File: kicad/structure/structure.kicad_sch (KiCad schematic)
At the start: 12 parts, among them J10 Conn_01x04_Socket, J11 Conn_01x04_Socket, J12 Conn_01x03_Socket, J13 Conn_01x06_Socket, J14 Conn_01x06_Socket, J3 Conn_01x08_Socket, J4 Conn_01x05_Socket, J5 Conn_01x03_Socket, J6 Conn_01x06_Socket, J7 Conn_01x04_Socket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

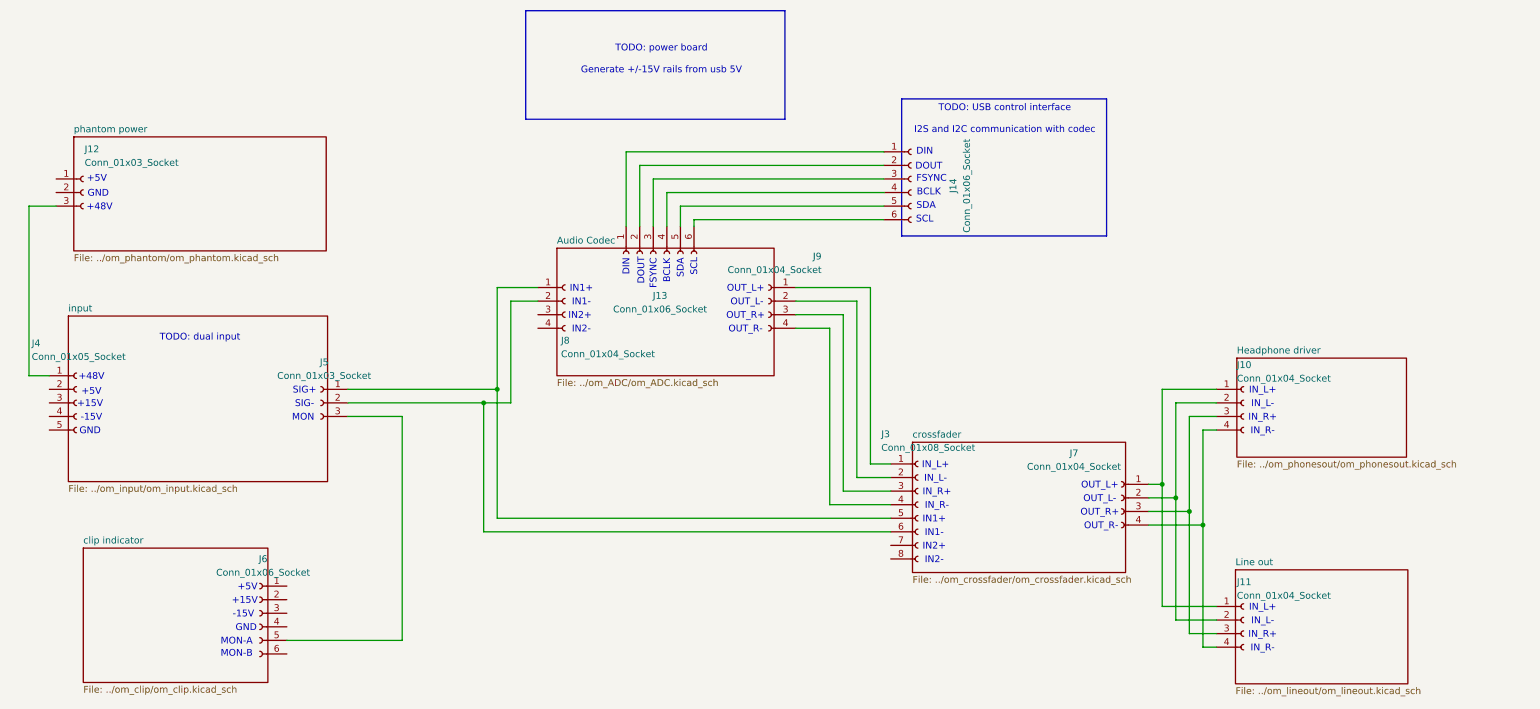
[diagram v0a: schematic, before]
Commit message: added structure and dual input
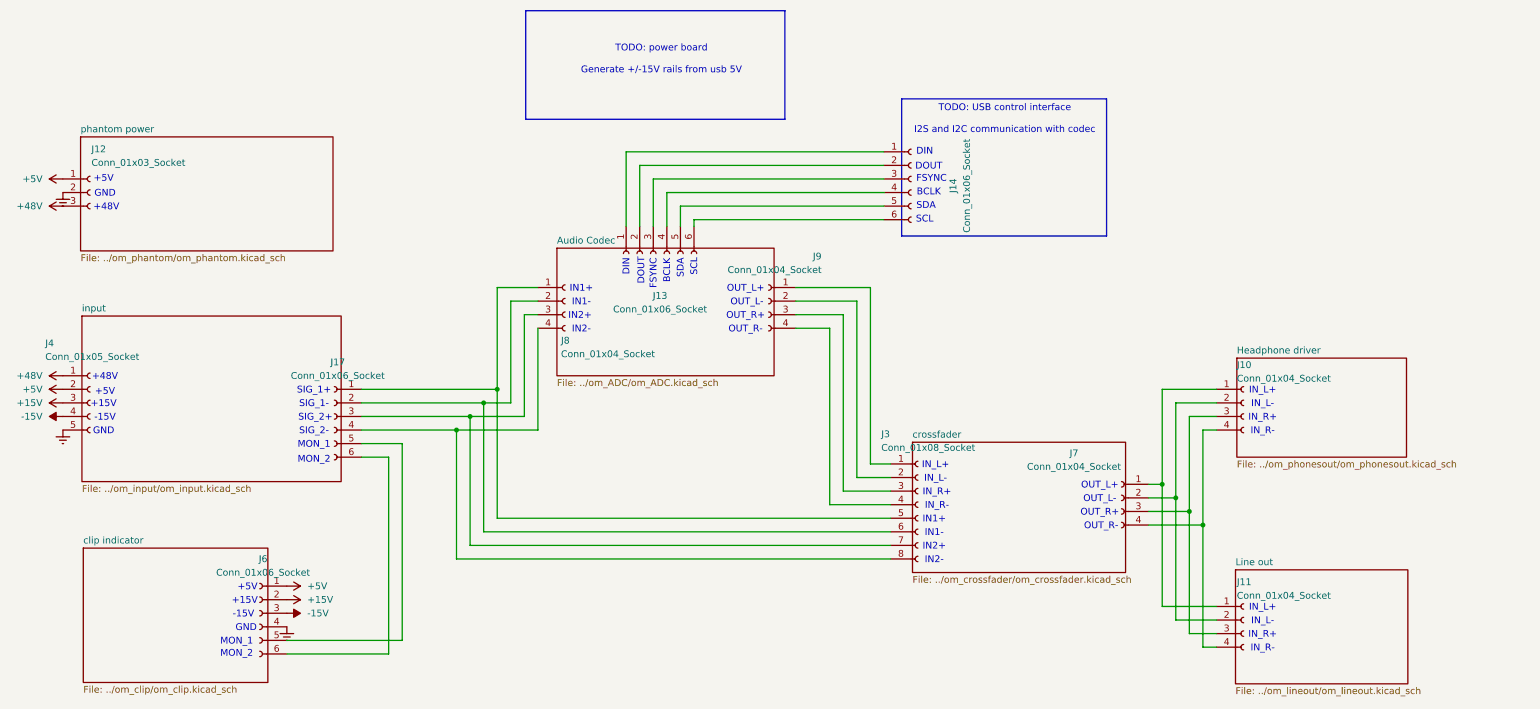
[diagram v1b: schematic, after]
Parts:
- removed J5: Conn_01x03_Socket, symbol Connector:Conn_01x03_Socket
- added J17: Conn_01x06_Socket, symbol Connector:Conn_01x06_Socket
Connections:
- net +48V: now reaches J12.3 (Pin_3), J4.1 (Pin_1)
- net +5V: now reaches J4.2 (Pin_2)
- net +5V: now also J12.1 (Pin_1), J6.1 (Pin_1)
- net +15V: now reaches J4.3 (Pin_3)
- net +15V: now also J6.2 (Pin_2)
- net -15V: now reaches J4.4 (Pin_4)
- net -15V: now also J6.3 (Pin_3)
- net Earth: now reaches J4.5 (Pin_5)
- net Earth: now also J12.2 (Pin_2), J6.4 (Pin_4)
- net at J3.5 (Pin_5), J8.1 (Pin_1): now also J17.1 (Pin_1)
- net at J3.6 (Pin_6), J8.2 (Pin_2): now also J17.2 (Pin_2)
- net at J8.3 (Pin_3): now also J3.7 (Pin_7), J17.3 (Pin_3)
- net at J8.4 (Pin_4): now also J3.8 (Pin_8), J17.4 (Pin_4)
- net at J6.5 (Pin_5): now also J17.5 (Pin_5)
- net at J6.6 (Pin_6): now also J17.6 (Pin_6)
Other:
- note added: "MON_1"
- note added: "MON_2"
- note added: "SIG_1+"
- note added: "SIG_1-"
- note added: "SIG_2+"
- note added: "SIG_2-"
- note removed: "MON"
- note removed: "MON-A"
- note removed: "MON-B"
- note removed: "SIG+"
- note removed: "SIG-"
- note removed: "TODO: dual input"
- moved on the sheet: J12, J4

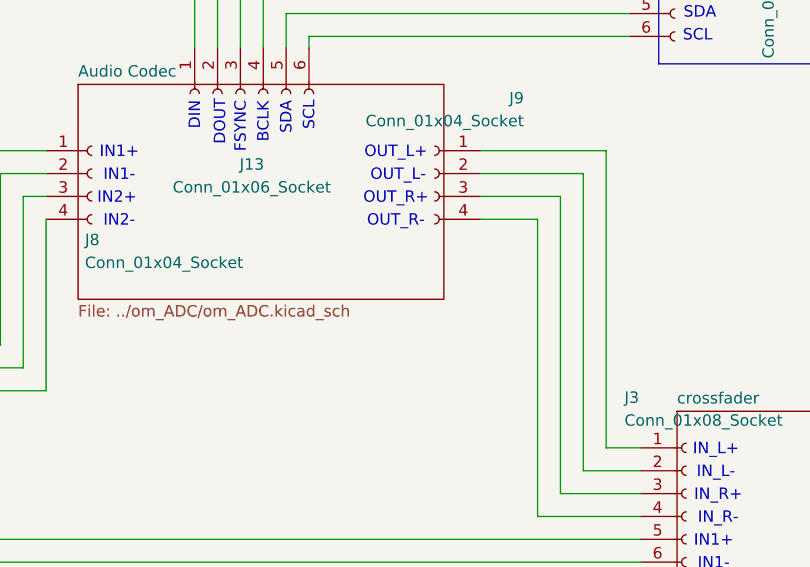
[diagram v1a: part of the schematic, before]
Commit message: direct monitor switch (#5)
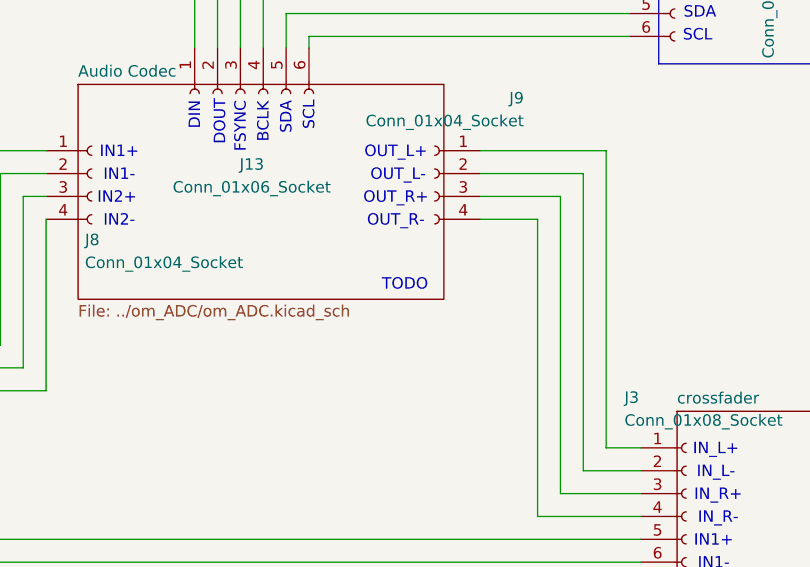
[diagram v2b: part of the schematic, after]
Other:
- note added: "TODO"
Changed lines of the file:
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@@
+		)
+	)
+	(text "TODO"
+		(exclude_from_sim no)
+		(at 151.638 89.916 0)
+		(effects
+			(font
+				(size 1.27 1.27)
+			)
 		)
 	)

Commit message: net labels
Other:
- note added: "phantom"
- note removed: "+48V"
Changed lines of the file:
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@@
 		)
 	)
-	(text "+48V"
+	(text "phantom"
 		(exclude_from_sim no)
-		(at 30.734 91.694 0)
+		(at 33.02 91.694 0)
 		(effects
 			(font
@@
 		)
 	)
-	(text "+48V"
+	(text "phantom"
 		(exclude_from_sim no)
-		(at 30.988 59.944 0)
+		(at 33.02 59.944 0)
 		(effects
 			(font

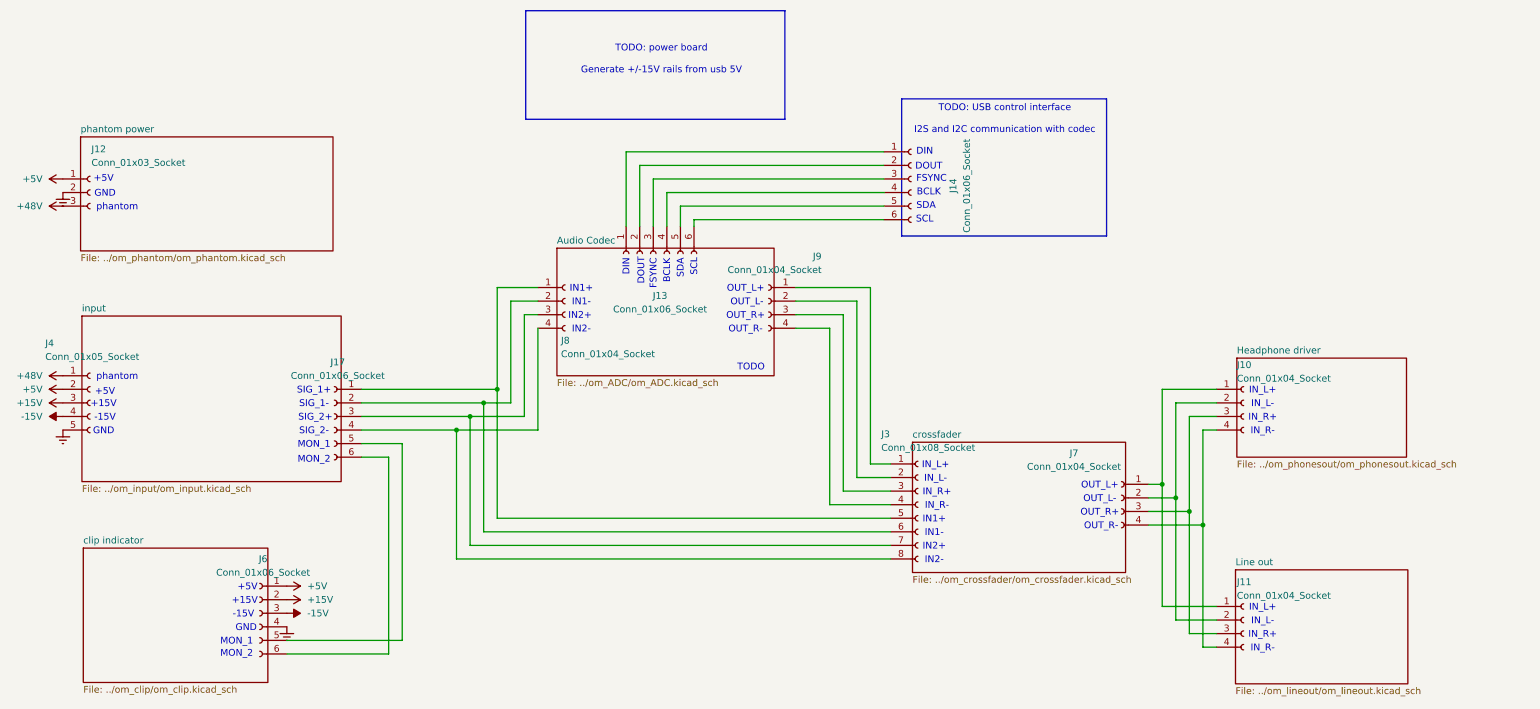
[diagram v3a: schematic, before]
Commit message: line output gain staging
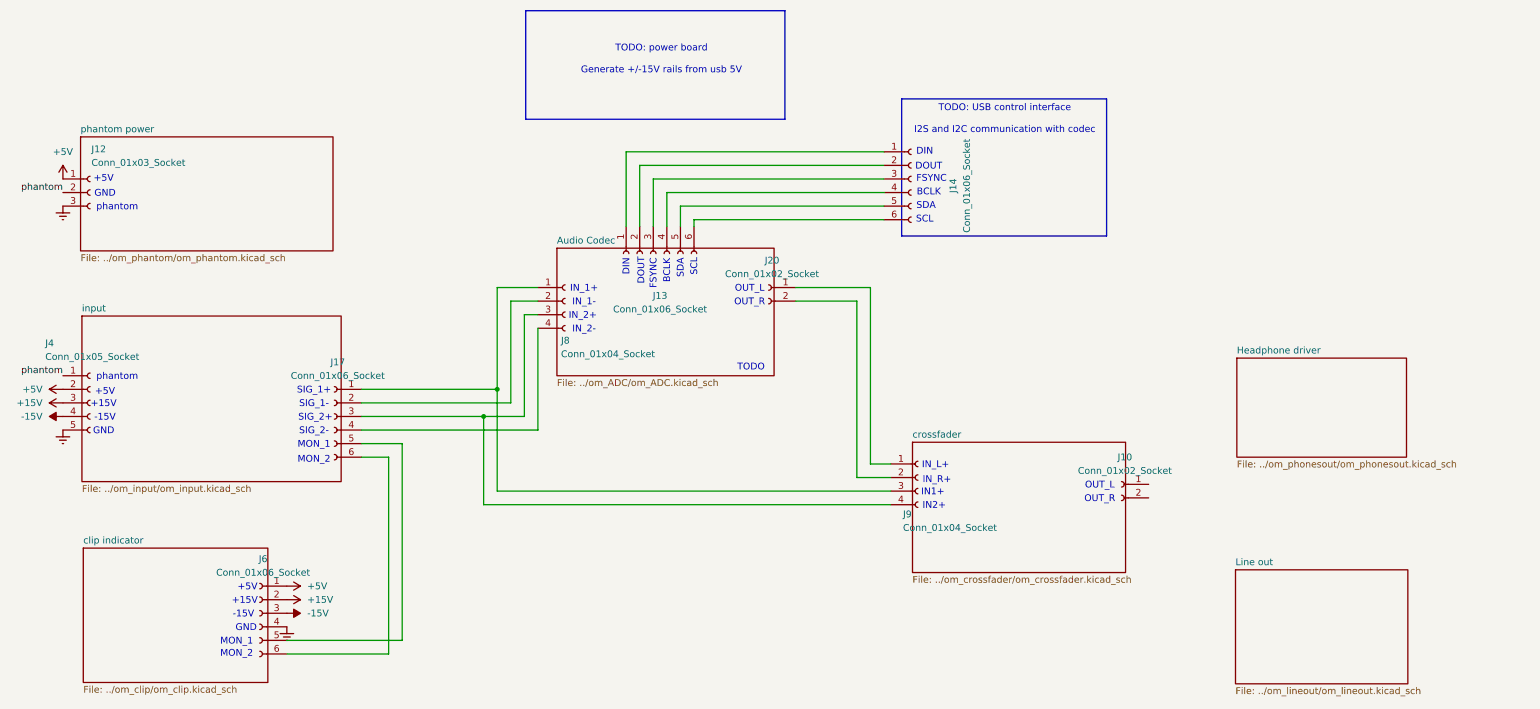
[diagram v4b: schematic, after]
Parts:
- removed J10, J11, J7: Conn_01x04_Socket, symbol Connector:Conn_01x04_Socket
- removed J3: Conn_01x08_Socket, symbol Connector:Conn_01x08_Socket
- added J10, J20: Conn_01x02_Socket, symbol Connector:Conn_01x02_Socket
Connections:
- net Earth: now also J12.3 (Pin_3); no longer J12.2 (Pin_2)
- net at J9.1 (Pin_1): now also J20.1 (Pin_1)
- net at J9.2 (Pin_2): now also J20.2 (Pin_2)
- net at J9.3 (Pin_3): now also J17.1 (Pin_1), J8.1 (Pin_1)
- net at J9.4 (Pin_4): now also J17.3 (Pin_3), J8.3 (Pin_3)
- net +48V renamed phantom
- net phantom: now also J12.2 (Pin_2); no longer J12.3 (Pin_3)
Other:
- note added: "IN_1+"
- note added: "IN_1-"
- note added: "IN_2+"
- note added: "IN_2-"
- note added: "OUT_L"
- note added: "OUT_R"
- note removed: "IN1-"
- note removed: "IN2-"
- note removed: "IN_L-"
- note removed: "IN_R-"
- note removed: "OUT_L+"
- note removed: "OUT_L-"
- note removed: "OUT_R+"
- note removed: "OUT_R-"

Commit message: line out connections
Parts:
- added J22: Conn_01x05_Socket, symbol Connector:Conn_01x05_Socket
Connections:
- net +15V: now also J22.1 (Pin_1)
- net -15V: now also J22.2 (Pin_2)
- net Earth: now also J22.3 (Pin_3)
- net at J10.1 (Pin_1): now also J22.4 (Pin_4)
- net at J10.2 (Pin_2): now also J22.5 (Pin_5)
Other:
- note added: "IN_L"
- note added: "IN_R"

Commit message: headphone driver (#7)
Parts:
- added J25: Conn_01x05_Socket, symbol Connector:Conn_01x05_Socket
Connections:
- net +15V: now also J25.1 (Pin_1)
- net -15V: now also J25.2 (Pin_2)
- net Earth: now also J25.3 (Pin_3)
- net at J10.1 (Pin_1), J22.4 (Pin_4): now also J25.4 (Pin_4)
- net at J10.2 (Pin_2), J22.5 (Pin_5): now also J25.5 (Pin_5)
